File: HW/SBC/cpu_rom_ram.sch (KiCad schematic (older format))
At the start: 6 parts, among them U1 WD65C02PLCC44, U2 28C256, U3 AS6C62256A

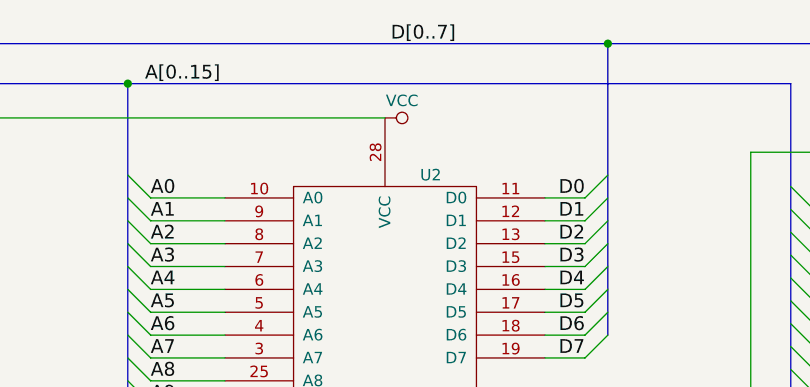
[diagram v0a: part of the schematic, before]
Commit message: Added CPLD to schematics. Updates rest of schematics to use CPLD
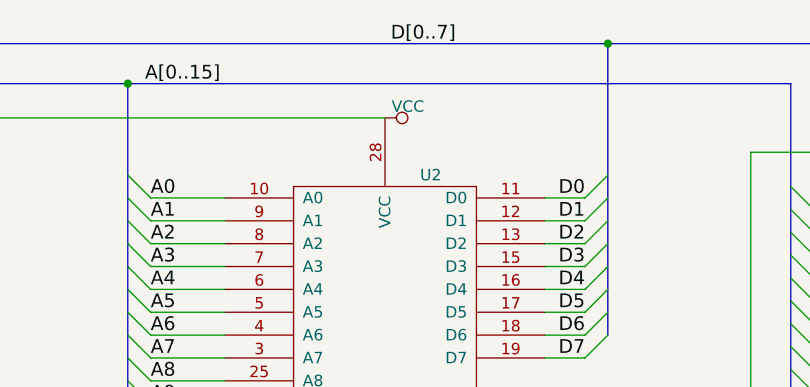
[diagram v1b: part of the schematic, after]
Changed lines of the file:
@@
 $Descr A4 11693 8268
 encoding utf-8
-Sheet 2 8
+Sheet 2 7
 Title "CPU, ROM and RAM"
 Date "2017-03-25"
@@
 F 3 "" H 5775 3550 50  0001 C CNN
 	1    5775 3550
-	0    1    1    0
-$EndComp
-$Comp
-L VCC #PWR04
-U 1 1 5924DCC6
-P 5775 1050
-F 0 "#PWR04" H 5775 900 50  0001 C CNN
-F 1 "VCC" V 5700 1125 50  0000 C CNN
-F 2 "" H 5775 1050 50  0001 C CNN
-F 3 "" H 5775 1050 50  0001 C CNN
-	1    5775 1050
 	0    1    1    0
 $EndComp
@@
 $EndComp
 $Comp
-L GND #PWR05
+L GND #PWR04
 U 1 1 5939C93B
 P 8450 3200
-F 0 "#PWR05" H 8450 2950 50  0001 C CNN
+F 0 "#PWR04" H 8450 2950 50  0001 C CNN
 F 1 "GND" H 8450 3050 50  0000 C CNN
 F 2 "" H 8450 3200 50  0001 C CNN
@@
 	1    8450 3200
 	0    -1   -1   0
-$EndComp
-$Comp
-L VCC #PWR06
-U 1 1 5939CBCE
-P 8450 1200
-F 0 "#PWR06" H 8450 1050 50  0001 C CNN
-F 1 "VCC" H 8450 1350 50  0000 C CNN
-F 2 "" H 8450 1200 50  0001 C CNN
-F 3 "" H 8450 1200 50  0001 C CNN
-	1    8450 1200
-	1    0    0    -1
 $EndComp
 Text HLabel 1300 2850 0    60   Input ~ 0
@@
 NoConn ~ 1525 2650
 NoConn ~ 1525 2750
+$Comp
+L VCC #PWR05
+U 1 1 5A161C1A
+P 8450 1200
+F 0 "#PWR05" H 8450 1050 50  0001 C CNN
+F 1 "VCC" H 8450 1350 50  0000 C CNN
+F 2 "" H 8450 1200 50  0001 C CNN
+F 3 "" H 8450 1200 50  0001 C CNN
+	1    8450 1200
+	1    0    0    -1
+$EndComp
+$Comp
+L VCC #PWR06
+U 1 1 5A163630
+P 5775 1050
+F 0 "#PWR06" H 5775 900 50  0001 C CNN
+F 1 "VCC" V 5725 1150 50  0000 C CNN
+F 2 "" H 5775 1050 50  0001 C CNN
+F 3 "" H 5775 1050 50  0001 C CNN
+	1    5775 1050
+	0    1    1    0
+$EndComp
 $EndSCHEMATC
